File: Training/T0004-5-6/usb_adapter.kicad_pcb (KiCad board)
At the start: 2 copper layers, 50.8 x 25.4 mm, 23 parts, among them J1 modular8_rev3_comms_out, P1 USB_OTG, U1 FT231XS, U2 TE_1825058-1

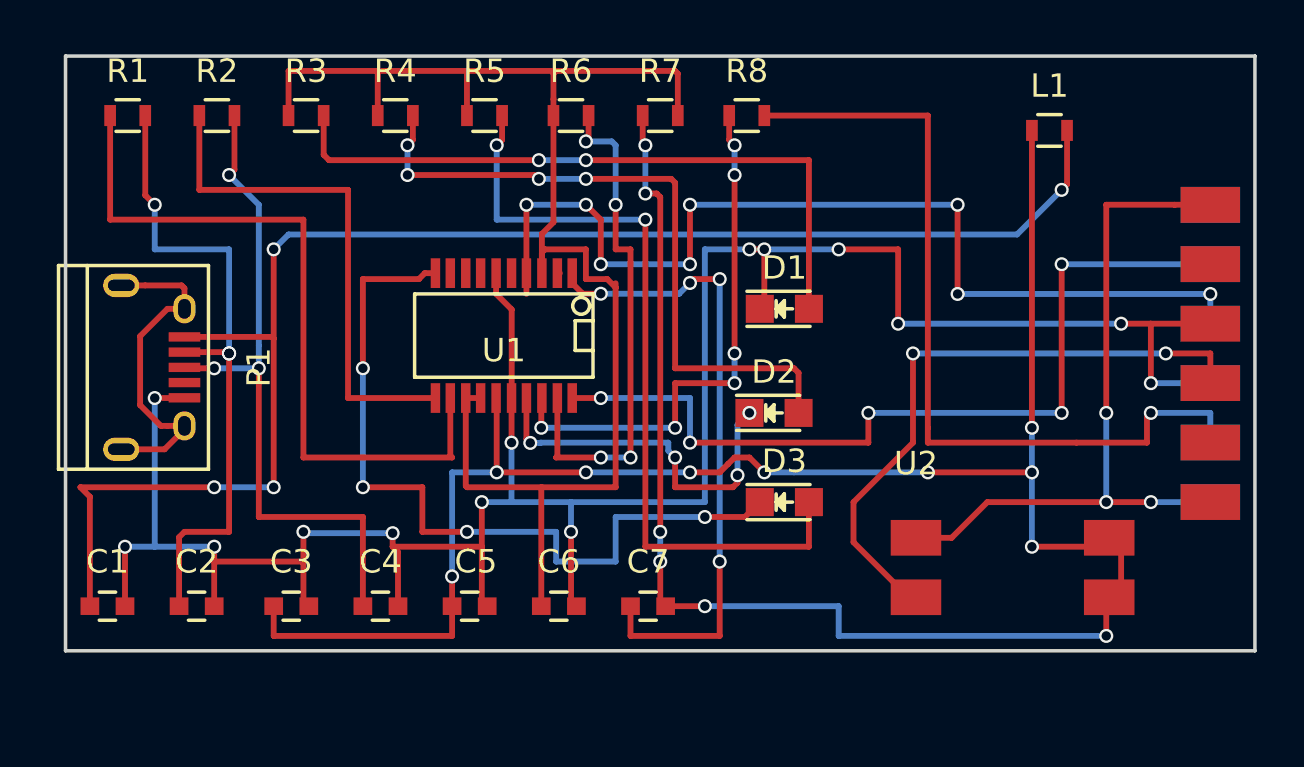
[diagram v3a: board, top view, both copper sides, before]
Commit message: Updated USB footprint and rails to 5V
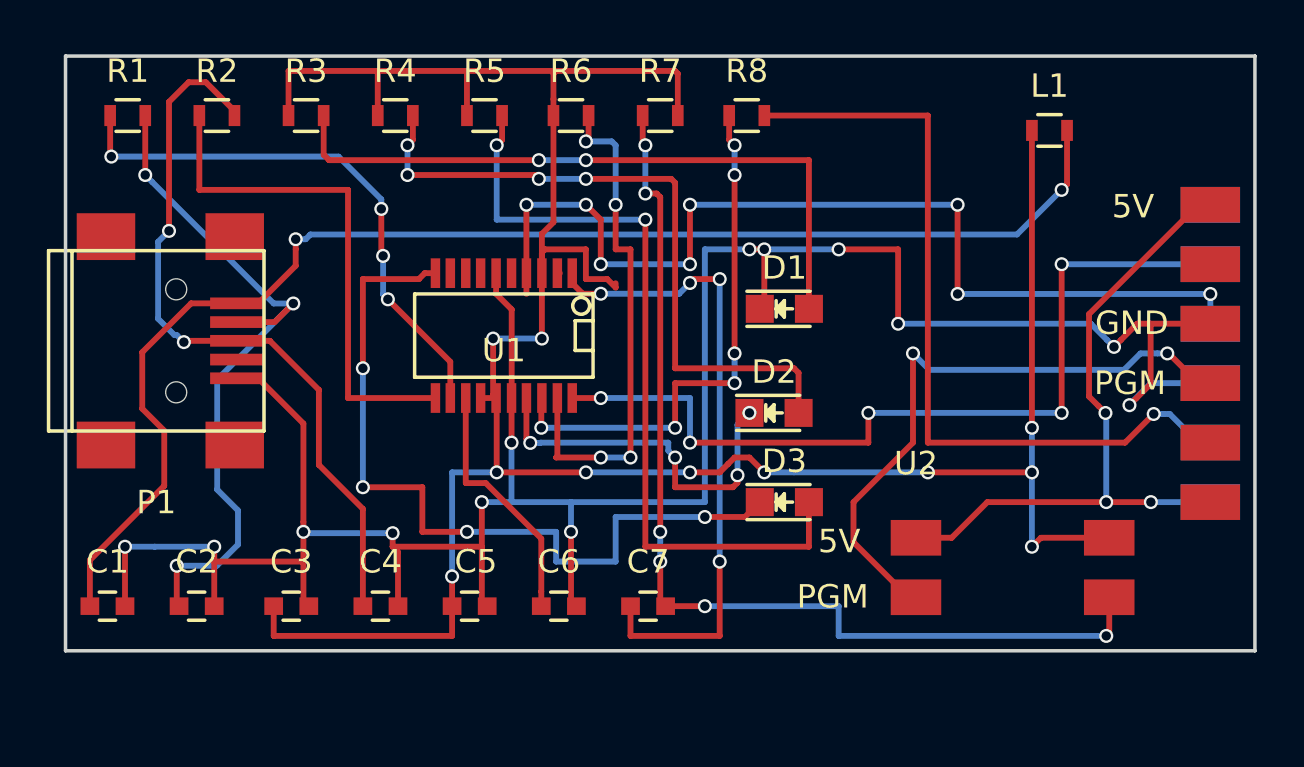
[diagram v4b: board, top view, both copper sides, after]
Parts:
- P1: footprint Connect:USB_Micro-B -> Connect:USB_Mini-B
- moved P1 1.19 mm to (130.9, 113.8), turned to 0 degrees
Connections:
- R3 pad 1: +3V3 -> +5V
- R4 pad 1: +3V3 -> +5V
- R5 pad 1: +3V3 -> +5V
- R6 pad 1: +3V3 -> +5V
- R7 pad 2: +3V3 -> +5V
- U1 pad 14: +3V3 -> +5V
- U1 pad 3: +3V3 -> +5V
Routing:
- net +3V3: track 63.2 -> 10.7 mm
- net +5V: track 68.1 -> 113.0 mm, vias 9 -> 11
- net Net-(P1-Pad6): track 14.4 -> 0.00 mm
- net Net-(R1-Pad1): track 31.8 -> 23.8 mm, vias 0 -> 4
- net Net-(C1-Pad1): track 64.8 -> 58.0 mm, vias 4 -> 2
- net GND: track 106.5 -> 110.6 mm, vias 14 -> 13
- net Net-(C2-Pad1): track 28.2 -> 30.6 mm
- net Net-(C4-Pad1): track 29.2 -> 31.5 mm, vias 3 -> 2
- net /POWER_OUT: track 30.3 -> 28.7 mm
- net Net-(J1-Pad10): track 35.5 -> 34.0 mm
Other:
- board text added: "5V"
- board text added: "GND"
- board text added: "PGM"
- board text added: "RX"
- board text added: "TX"
- board text added: "TXDEN"
